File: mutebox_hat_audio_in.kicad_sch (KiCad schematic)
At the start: 39 parts, among them J1 GPIO, J3 RCJ-042, J4 RCJ-042, U2 74LVC157, U3 PCM1862DBT, Y3 XO32

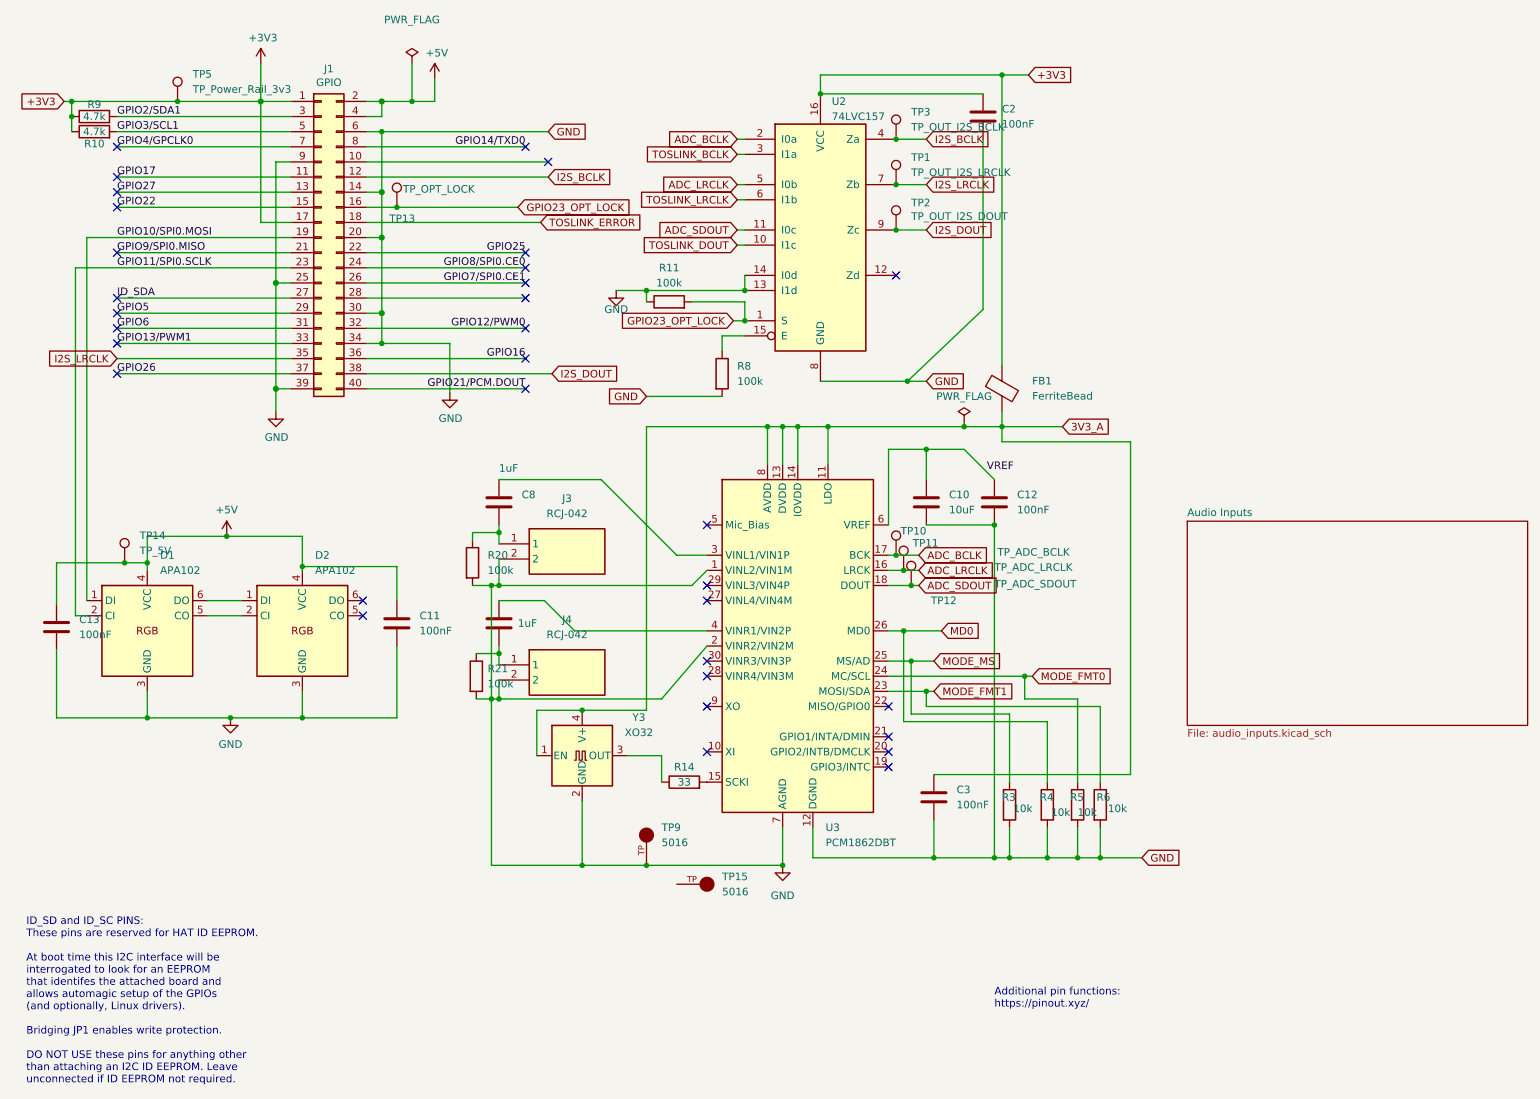
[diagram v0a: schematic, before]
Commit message: Fixed dotstar positioning.  Minor changes to PCB
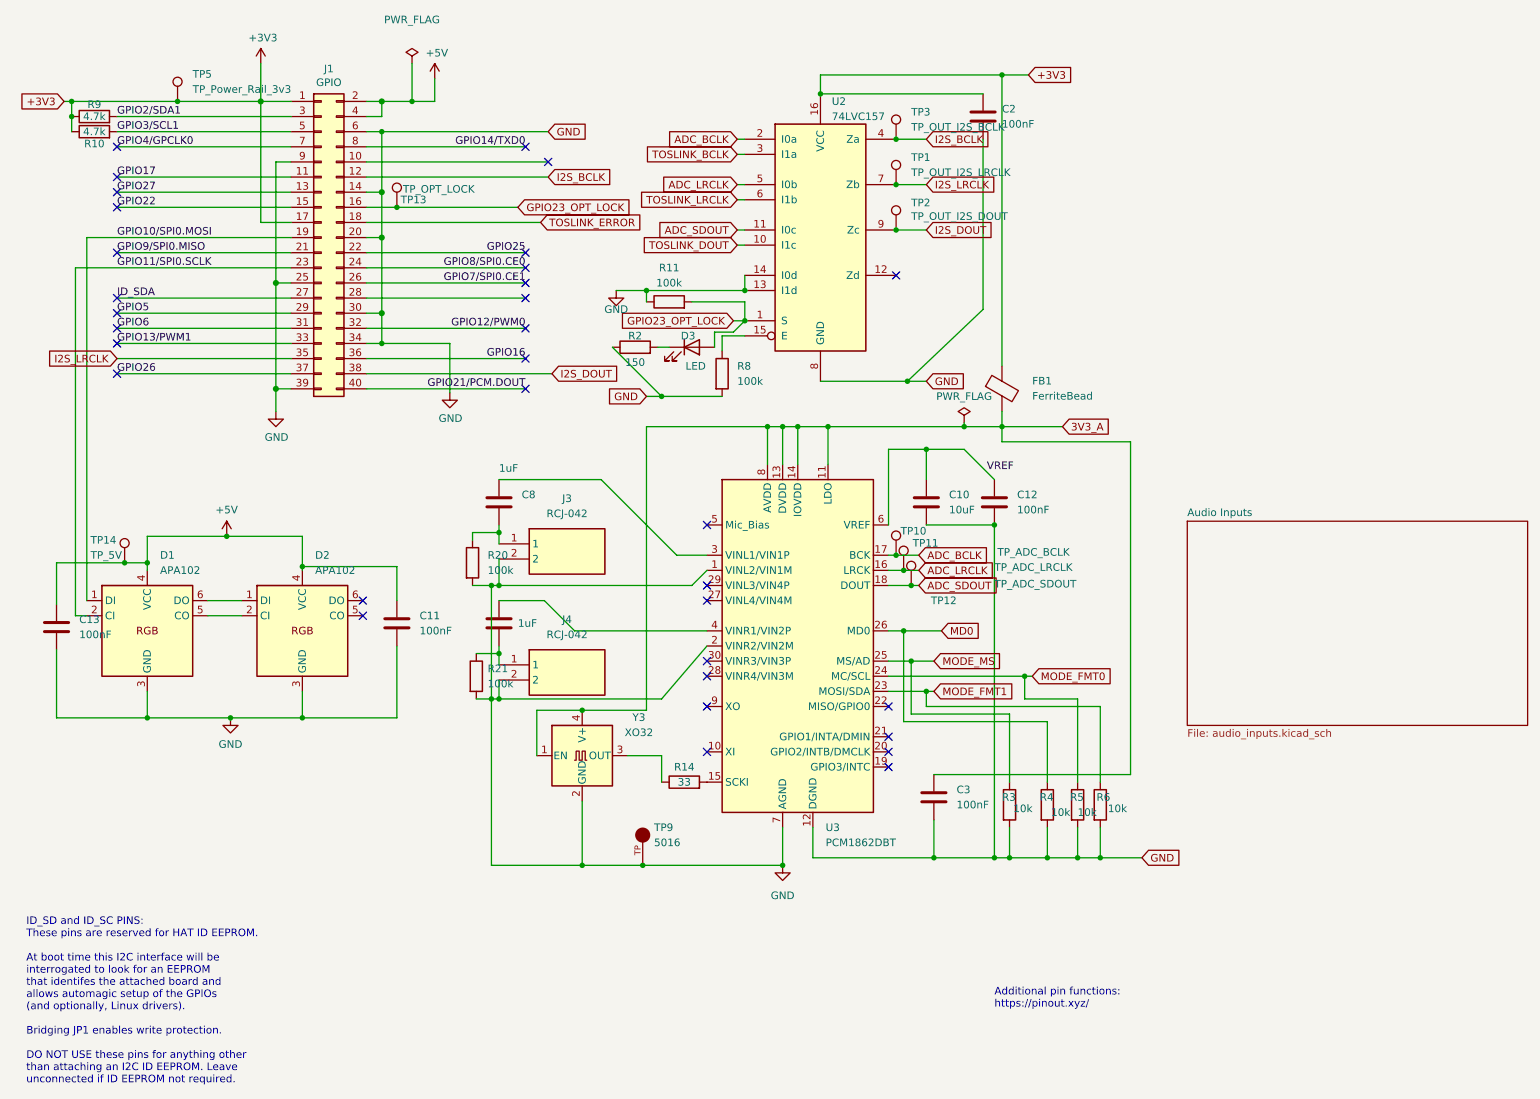
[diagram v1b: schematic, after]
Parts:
- removed TP15: 5016, 5016:KEYSTONE_5016, symbol TestPoint:5016
- added D3: LED, LED_SMD:LED_0805_2012Metric_Pad1.15x1.40mm_HandSolder, symbol Device:LED
- added R2: 150, Resistor_SMD:R_0805_2012Metric_Pad1.20x1.40mm_HandSolder, symbol Device:R
- TP9: footprint 5016:KEYSTONE_5016 -> Connector:KEYSTONE_5016
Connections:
- net GND: now also R2.1
- net GPIO23_OPT_LOCK: now also D3.2 (A)
- new net: D3.1 (K), R2.2

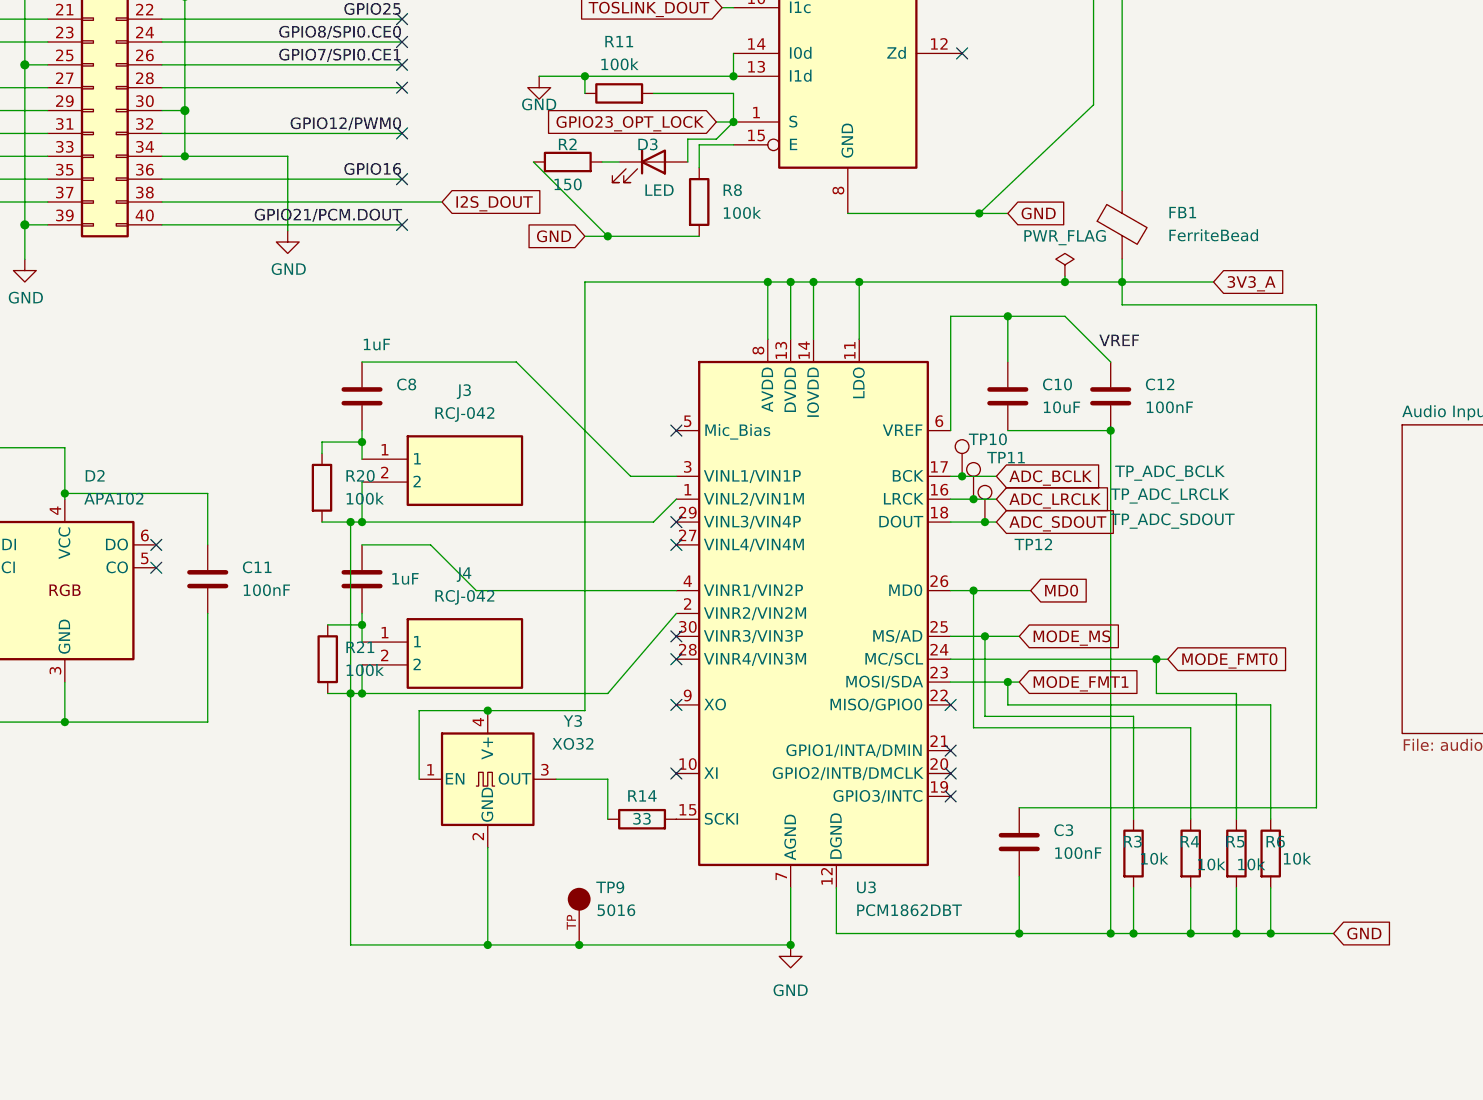
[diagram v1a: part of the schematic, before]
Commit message: Rewired MS to 3v3a instead of GND
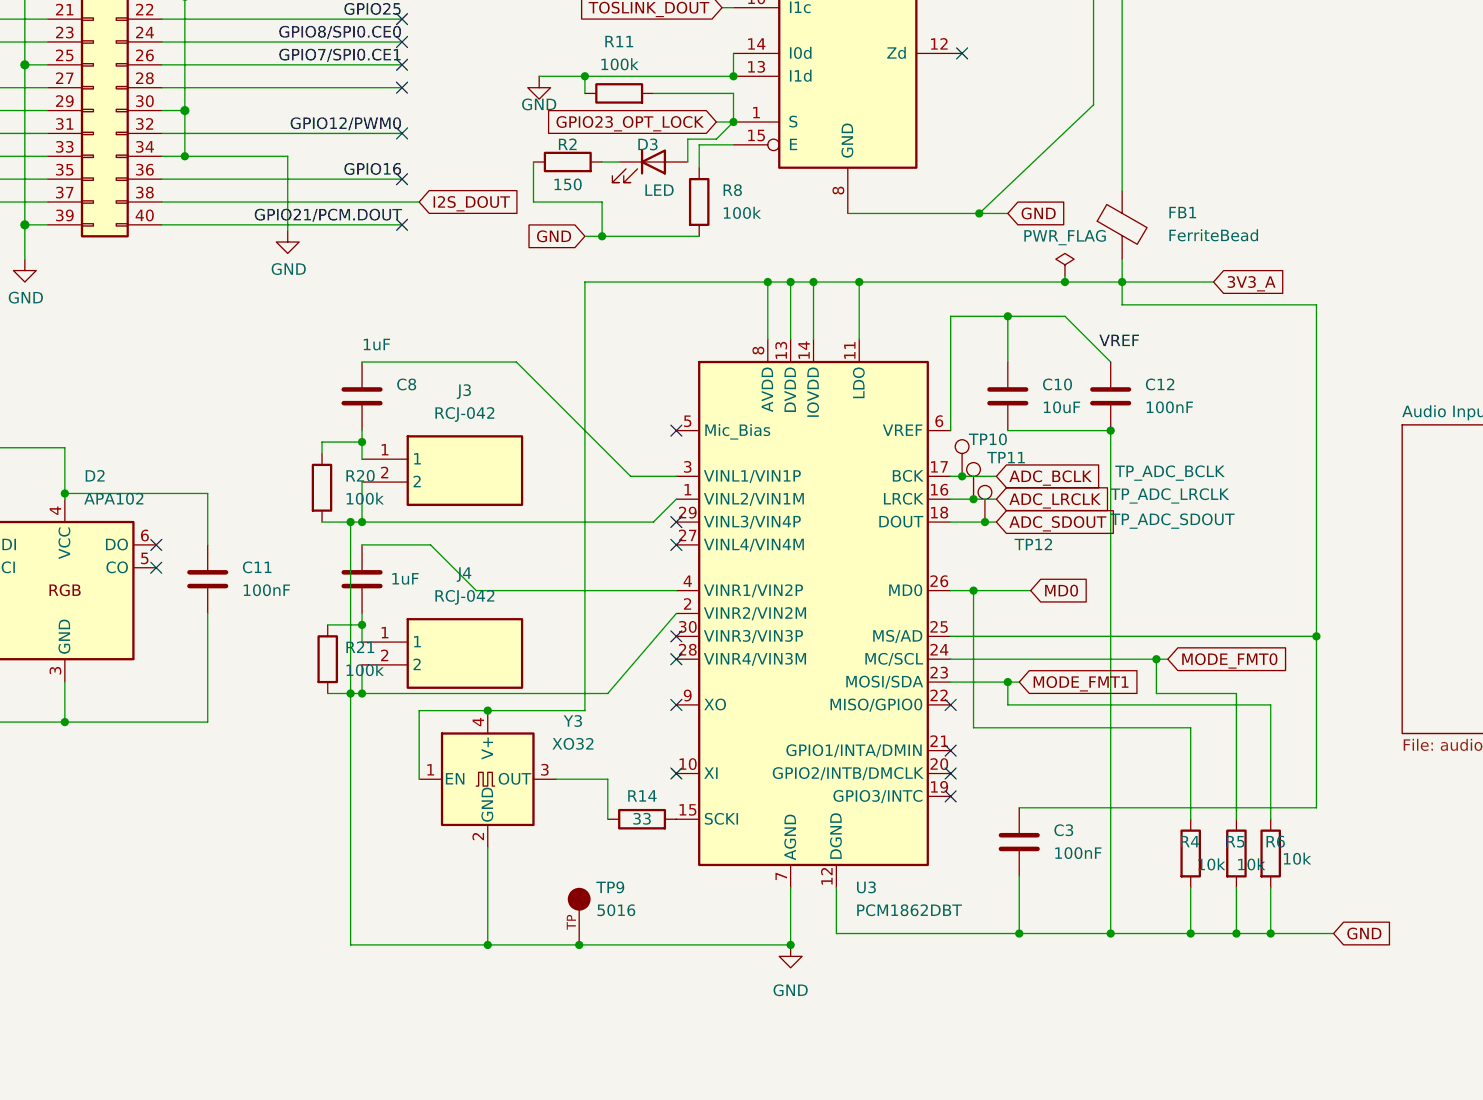
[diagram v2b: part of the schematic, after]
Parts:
- removed R3: 10k, Resistor_SMD:R_0805_2012Metric_Pad1.20x1.40mm_HandSolder, symbol Device:R
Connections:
- net MODE_MS is gone; now on net 3V3_A: U3.25 (MS/AD)
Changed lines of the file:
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@@
 	)
 	(junction
-		(at 165.1 121.92)
-		(diameter 0)
-		(color 0 0 0 0)
-	)
-	(junction
 		(at 196.85 154.94)
 		(diameter 0)
@@
 	)
 	(junction
+		(at 122.555 77.47)
+		(diameter 0)
+		(color 0 0 0 0)
+	)
+	(junction
 		(at 168.91 154.94)
 		(diameter 0)
@@
 	)
 	(junction
-		(at 123.19 77.47)
-		(diameter 0)
-		(color 0 0 0 0)
-	)
-	(junction
 		(at 167.64 127)
 		(diameter 0)
@@
 	)
 	(junction
+		(at 201.93 121.92)
+		(diameter 0)
+		(color 0 0 0 0)
+	)
+	(junction
 		(at 163.83 106.68)
 		(diameter 0)
@@
 	)
 	(junction
-		(at 181.61 154.94)
-		(diameter 0)
-		(color 0 0 0 0)
-	)
-	(junction
 		(at 76.2 50.8)
 		(diameter 1.016)
@@
 	(wire
 		(pts
-			(xy 165.1 130.81) (xy 181.61 130.81)
+			(xy 120.65 59.69) (xy 137.16 59.69)
 		)
 		(stroke
@@
 	(wire
 		(pts
-			(xy 120.65 59.69) (xy 137.16 59.69)
+			(xy 122.555 77.47) (xy 133.35 77.47)
 		)
 		(stroke
@@
 	(wire
 		(pts
-			(xy 181.61 149.86) (xy 181.61 154.94)
-		)
-		(stroke
-			(width 0)
-			(type default)
-		)
-	)
-	(wire
-		(pts
 			(xy 91.44 101.6) (xy 91.44 100.33)
 		)
@@
 	(wire
 		(pts
-			(xy 114.935 69.215) (xy 123.19 77.47)
-		)
-		(stroke
-			(width 0)
-			(type default)
-		)
-	)
-	(wire
-		(pts
 			(xy 73.66 48.26) (xy 102.87 48.26)
 		)
@@
 	(wire
 		(pts
+			(xy 201.93 121.92) (xy 201.93 140.97)
+		)
+		(stroke
+			(width 0)
+			(type default)
+		)
+	)
+	(wire
+		(pts
 			(xy 163.83 116.84) (xy 170.18 116.84)
 		)
@@
 	(wire
 		(pts
-			(xy 181.61 130.81) (xy 181.61 142.24)
-		)
-		(stroke
-			(width 0)
-			(type default)
-		)
-	)
-	(wire
-		(pts
 			(xy 76.2 68.58) (xy 73.66 68.58)
 		)
@@
 	(wire
 		(pts
-			(xy 179.07 154.94) (xy 181.61 154.94)
-		)
-		(stroke
-			(width 0)
-			(type default)
-		)
-	)
-	(wire
-		(pts
 			(xy 31.75 33.02) (xy 60.96 33.02)
 		)
@@
 	(wire
 		(pts
+			(xy 114.935 69.215) (xy 114.935 73.66)
+		)
+		(stroke
+			(width 0)
+			(type default)
+		)
+	)
+	(wire
+		(pts
 			(xy 173.99 86.36) (xy 179.07 91.44)
 		)
@@
 	(wire
 		(pts
-			(xy 181.61 154.94) (xy 187.96 154.94)
+			(xy 179.07 154.94) (xy 187.96 154.94)
 		)
 		(stroke
@@
 	(wire
 		(pts
+			(xy 114.935 73.66) (xy 122.555 73.66)
+		)
+		(stroke
+			(width 0)
+			(type default)
+		)
+	)
+	(wire
+		(pts
 			(xy 31.75 73.66) (xy 60.96 73.66)
 		)
@@
 	(wire
 		(pts
-			(xy 87.63 68.58) (xy 87.63 76.835)
+			(xy 122.555 73.66) (xy 122.555 77.47)
 		)
 		(stroke
@@
 	(wire
 		(pts
-			(xy 149.86 74.93) (xy 164.465 74.93)
+			(xy 87.63 68.58) (xy 87.63 76.835)
 		)
 		(stroke
@@
 	(wire
 		(pts
-			(xy 163.83 116.84) (xy 163.83 132.08)
+			(xy 149.86 74.93) (xy 164.465 74.93)
 		)
 		(stroke
@@
 	(wire
 		(pts
-			(xy 123.19 77.47) (xy 133.35 77.47)
+			(xy 163.83 116.84) (xy 163.83 132.08)
 		)
 		(stroke
@@
 	(wire
 		(pts
-			(xy 36.83 131.445) (xy 50.8 131.445)
+			(xy 120.65 77.47) (xy 122.555 77.47)
 		)
 		(stroke
@@
 	(wire
 		(pts
-			(xy 120.65 77.47) (xy 123.19 77.47)
+			(xy 36.83 131.445) (xy 50.8 131.445)
 		)
 		(stroke
@@
 	(wire
 		(pts
-			(xy 161.29 121.92) (xy 165.1 121.92)
+			(xy 161.29 121.92) (xy 201.93 121.92)
 		)
 		(stroke
@@
 	(wire
 		(pts
-			(xy 165.1 121.92) (xy 165.1 130.81)
-		)
-		(stroke
-			(width 0)
-			(type default)
-		)
-	)
-	(wire
-		(pts
 			(xy 73.66 45.72) (xy 78.74 45.72)
 		)
@@
 	(wire
 		(pts
-			(xy 73.66 73.66) (xy 104.775 73.66)
+			(xy 73.66 73.66) (xy 102.235 73.66)
 		)
 		(stroke
@@
 	(wire
 		(pts
-			(xy 201.93 85.09) (xy 201.93 140.97)
+			(xy 201.93 85.09) (xy 201.93 121.92)
 		)
 		(stroke
@@
 	(wire
 		(pts
-			(xy 165.1 121.92) (xy 168.91 121.92)
-		)
-		(stroke
-			(width 0)
-			(type default)
-		)
-	)
-	(wire
-		(pts
 			(xy 184.15 124.46) (xy 185.42 124.46)
 		)
@@
 	(global_label "I2S_DOUT"
 		(shape input)
-		(at 104.775 73.66 0)
+		(at 102.235 73.66 0)
 		(fields_autoplaced yes)
 		(effects
@@
 		)
 		(property "Intersheetrefs" "${INTERSHEET_REFS}"
-			(at 116.7453 73.66 0)
+			(at 114.2053 73.66 0)
 			(effects
 				(font
@@
 		)
 	)
-	(global_label "MODE_MS"
-		(shape input)
-		(at 168.91 121.92 0)
-		(fields_autoplaced yes)
-		(effects
-			(font
-				(size 1.27 1.27)
-			)
-			(justify left)
-		)
-		(property "Intersheetrefs" "${INTERSHEET_REFS}"
-			(at 180.8197 121.92 0)
-			(effects
-				(font
-					(size 1.27 1.27)
-				)
-				(justify left)
-				(hide yes)
-			)
-		)
-	)
 	(global_label "TOSLINK_DOUT"
 		(shape input)
@@
 					(unit 1)
 				)
-			)
-		)
-	)
-	(symbol
-		(lib_id "Device:R")
-		(at 181.61 146.05 0)
-		(unit 1)
-		(exclude_from_sim no)
-		(in_bom yes)
-		(on_board yes)
-		(dnp no)
-		(property "Reference" "R3"
-			(at 180.34 144.78 0)
-			(effects
-				(font
-					(size 1.27 1.27)
-				)
-				(justify left)
-			)
-		)
-		(property "Value" "10k"
-			(at 182.245 146.685 0)
-			(effects
-				(font
-					(size 1.27 1.27)
-				)
-				(justify left)
-			)
-		)
-		(property "Footprint" "Resistor_SMD:R_0805_2012Metric_Pad1.20x1.40mm_HandSolder"
-			(at 179.832 146.05 90)
-			(effects
-				(font
-					(size 1.27 1.27)
-				)
-				(hide yes)
-			)
-		)
-		(property "Datasheet" "~"
-			(at 181.61 146.05 0)
-			(effects
-				(font
-					(size 1.27 1.27)
-				)
-				(hide yes)
-			)
-		)
-		(property "Description" "Resistor"
-			(at 181.61 146.05 0)
-			(effects
-				(font
-					(size 1.27 1.27)
-				)
-				(hide yes)
-			)
-		)
-		(property "LCSC" "C17414"
-			(at 181.61 146.05 0)
-			(effects
-				(font
-					(size 1.27 1.27)
-				)
-				(hide yes)
-			)
-		)
-		(pin "1"
-		)
-		(pin "2"
-		)
-		(instances
-			(project ""
-				(path "/e63e39d7-6ac0-4ffd-8aa3-1841a4541b55"
-					(reference "R3")
-					(unit 1)
-				)
